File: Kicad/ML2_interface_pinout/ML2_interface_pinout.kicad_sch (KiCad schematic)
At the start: 2 parts, among them J1 Conn_02x28_Row_Letter_Last, J2 Conn_02x31_Row_Letter_First

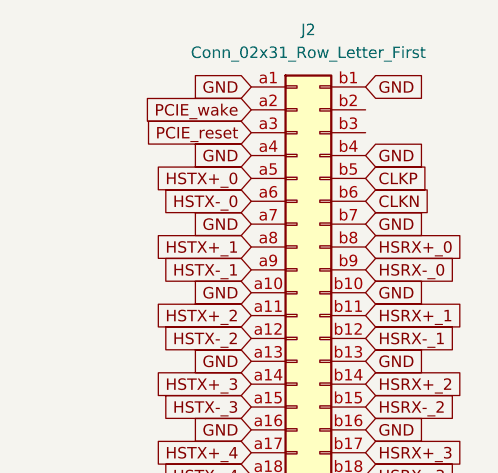
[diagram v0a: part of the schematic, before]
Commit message: Renaming some pins
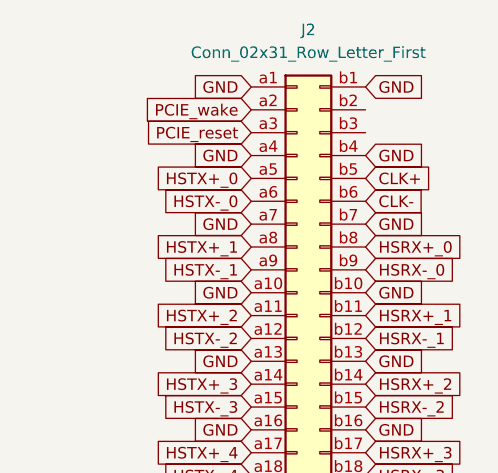
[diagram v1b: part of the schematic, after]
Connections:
- net CLKN renamed CLK-
- net CLKP renamed CLK+
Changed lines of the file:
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@@
 		)
 	)
-	(global_label "CLKN"
+	(global_label "CLK-"
 		(shape input)
 		(at 195.58 44.45 0)
@@
 		)
 		(property "Intersheetrefs" "${INTERSHEET_REFS}"
-			(at 203.4638 44.45 0)
+			(at 203.7057 44.45 0)
 			(effects
 				(font
@@
 		)
 	)
-	(global_label "CLKP"
+	(global_label "CLK+"
 		(shape input)
 		(at 195.58 41.91 0)
@@
 		)
 		(property "Intersheetrefs" "${INTERSHEET_REFS}"
-			(at 203.4033 41.91 0)
-			(effects
-				(font
+			(at 203.7057 41.91 0)
+			(effects
+				(font
